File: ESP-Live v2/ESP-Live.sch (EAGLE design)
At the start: 34 parts, among them CN1 USBSMD, IC2 AP2210K-3.3TRG1, IC3 ESP-12F, Y1 RESONATORSMD

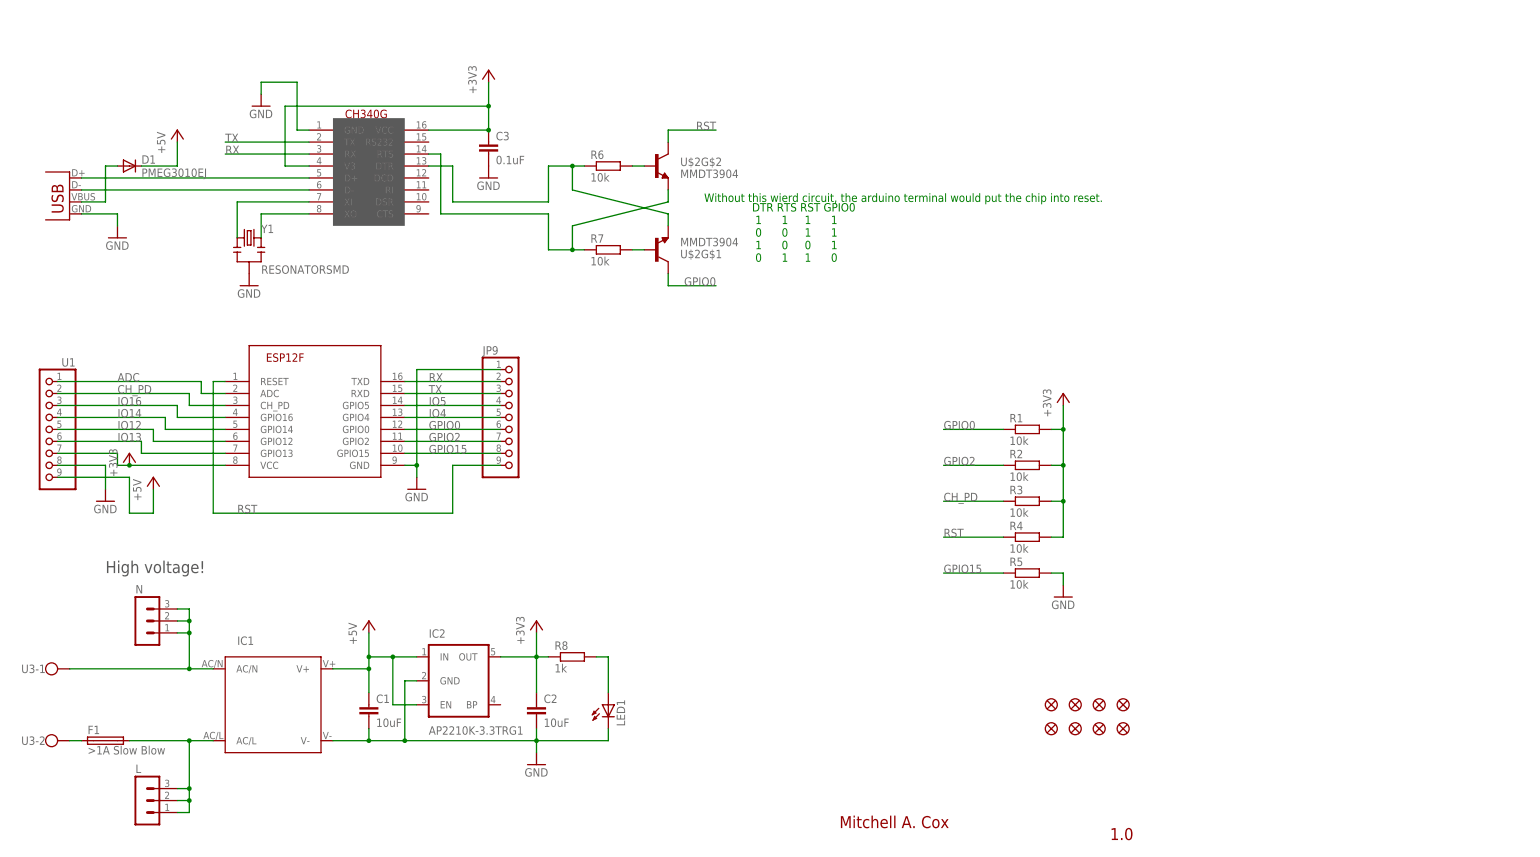
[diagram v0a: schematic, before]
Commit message: with batery charger
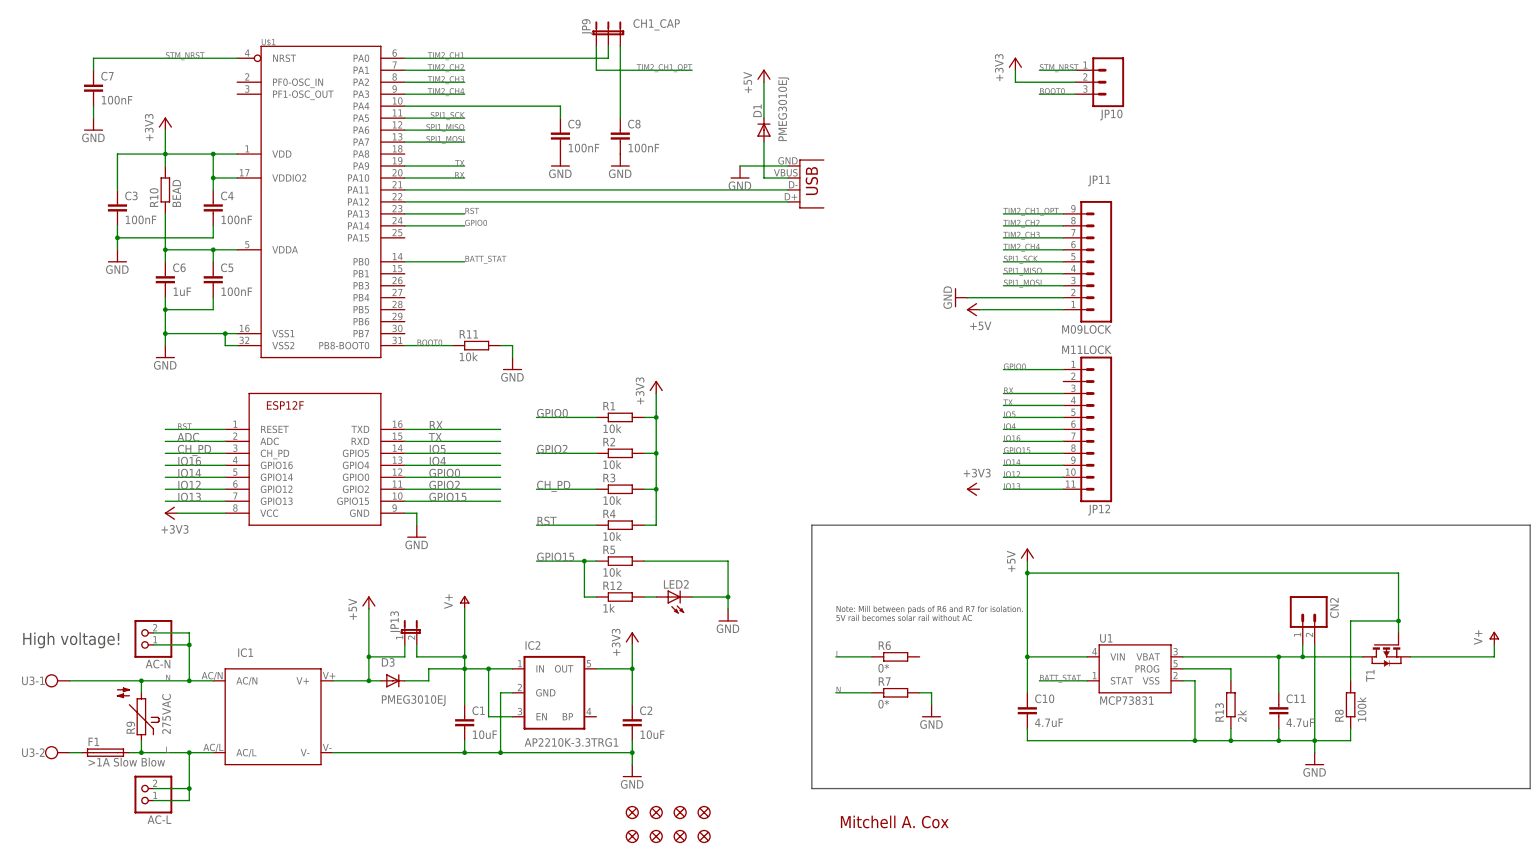
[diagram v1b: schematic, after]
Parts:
- removed L, N: (no value), con-lstb:MA03-1
- removed LED1: (no value), adafruit:LEDCHIPLED_0805
- removed U$2: MMDT3904, SparkFun:MMDT3904
- removed Y1: RESONATORSMD, SparkFun:RESONATORSMD
- added AC-L, AC-N: (no value), pinhead:PINHD-1X2
- added C10, C11: 4.7uF, rcl:C-EUC0805
- added C4, C5, C7, C8, C9: 100nF, rcl:C-EUC0603
- added C6: 1uF, rcl:C-EUC0805
- added CN2: (no value), SparkFun:M02-JST-2-PTH-NO_SILK
- added D3: PMEG3010EJ, SparkFun:DIODESOD
- added JP10: (no value), SparkFun:M03LOCK
- added JP11: M09LOCK, SparkFun:M09LOCK
- added JP12: M11LOCK, SparkFun:M11LOCK
- added JP13: (no value), SparkFun:JUMPER-2SMD-NO
- added LED2: (no value), adafruit:LEDCHIPLED_0805
- added R10: BEAD, rcl:R-EU_R0603
- added R11: 10k, rcl:R-EU_R0603
- added R12: 1k, rcl:R-EU_R0603
- added R13: 2k, rcl:R-EU_R0603
- added R9: 275VAC, varistor:P593
- added T1: (no value), zetex:PMOSSOT23
- C3: value 0.1uF -> 100nF; device rcl:C-EUC0805 -> rcl:C-EUC0603
- JP9: value (none) -> CH1_CAP; device adafruit:PINHD-1X9 -> SparkFun:JUMPER-31-2
- R1, R2, R3, R4, R5: device rcl:R-EU_M0805 -> rcl:R-EU_R0603
- R6, R7: value 10k -> 0*; device rcl:R-EU_M0805 -> rcl:R-EU_R2512
- R8: value 1k -> 100k; device rcl:R-EU_M0805 -> rcl:R-EU_R0603
- U$1: value CH340G -> STM32F042K; device usb-serial:CH340G -> stm32:STM32F042K
- U1: value (none) -> MCP73831; device adafruit:PINHD-1X9 -> SparkFun:MCP73831
- U3: device con-wago-500:W237-113 -> con-wago-500:W237-102
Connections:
- removed net N$15: R7.1, U$1.RTS, U$2G$2.E
- removed net N$16: CN1.D-, U$1.D-
- removed net N$21: U$1.XI, Y1.1
- removed net N$22: U$1.XO, Y1.3
- removed net N$4: LED1.A, R8.2
- removed net N$8: R7.2, U$2G$1.B
- new net BATT_STAT: U$1.PB0, U1.STAT
- new net BOOT0: JP10.3, R11.1, U$1.PB8-BOOT0
- new net L: AC-L.1, AC-L.2, F1.2, IC1.AC/L, R6.1, R9.1
- new net N: AC-N.1, AC-N.2, IC1.AC/N, R7.1, R9.2, U3-1.KL
- new net N$13: C11.1, CN2.1, T1.D, U1.VBAT
- new net N$6: CN1.D-, U$1.PA11
- new net N$7: CN1.D+, U$1.PA12
- new net SPI1_MISO: JP11.4, U$1.PA6
- new net SPI1_MOSI: JP11.3, U$1.PA7
- new net SPI1_SCK: JP11.5, U$1.PA5
- new net STM_NRST: C7.1, JP10.1, U$1.NRST
- new net TIM2_CH1: JP9.2, U$1.PA0
- new net TIM2_CH1_OPT: JP11.9, JP9.1
- new net TIM2_CH2: JP11.8, U$1.PA1
- new net TIM2_CH3: JP11.7, U$1.PA2
- new net TIM2_CH4: JP11.6, U$1.PA3
- new net V+: C1.1, D3.C, IC2.EN, IC2.IN, JP13.2, T1.S
- net +3V3: now also C4.1, JP10.2, R10.2, U$1.VDD, U$1.VDDIO2; no longer R8.1, U$1.V3, U$1.VCC, U1.7
- net +5V: now also C10.1, D3.A, JP11.1, JP13.1, R8.2, T1.G, U1.VIN; no longer C1.1, IC2.EN, IC2.IN, U1.9
- net ADC: no longer U1.1
- net CH_PD: no longer U1.2
- net GND: now also C10.2, C11.2, C4.2, C5.2, C6.2, C7.2, C8.2, C9.2, CN2.2, JP11.2, LED2.C, R11.2, R13.1, R7.2, R8.1, U$1.VSS1, U$1.VSS2, U1.VSS; no longer JP9.1, LED1.C, U$1.GND, U1.8, Y1.2
- net GPIO0: now also JP12.1, U$1.PA14; no longer JP9.6, U$2G$1.C
- net GPIO15: now also JP12.8, R12.1; no longer JP9.8
- net GPIO2: no longer JP9.7
- net IO12: now also JP12.10; no longer U1.5
- net IO13: now also JP12.11; no longer U1.6
- net IO14: now also JP12.9; no longer U1.4
- net IO16: now also JP12.7; no longer U1.3
- net IO4: now also JP12.6; no longer JP9.5
- net IO5: now also JP12.5; no longer JP9.4
- net N$10: now also LED2.A, R12.2; no longer R6.2, U$2G$2.B
- net N$11: now also C9.1, U$1.PA4; no longer R6.1, U$1.DTR, U$2G$1.E
- net N$12: now also C8.1, JP9.3; no longer CN1.D+, U$1.D+
- net N$2: now also C5.1, C6.1, R10.1, U$1.VDDA; no longer IC1.AC/N, N.1, N.2, N.3, U3-1.KL
- net N$3: now also R13.2, U1.PROG; no longer F1.2, IC1.AC/L, L.1, L.2, L.3
- net RST: now also U$1.PA13; no longer JP9.9, U$2G$2.C
- net RX: now also JP12.3, U$1.PA10; no longer JP9.2, U$1.RX
- net TX: now also JP12.4, U$1.PA9; no longer JP9.3, U$1.TX
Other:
- note added: "1A, 5.5V MAX"
- note added: "Note: Mill between pads of R6 and R7 for isolation. 5V rail becomes solar rail without AC"
- note removed: "1.0"
- note removed: "DTR RTS RST GPIO0 1 1 1 1 0 0 1 1 1 0 0 1 0 1 1 0"
- note removed: "Without this wierd circuit, the arduino terminal would put the chip into reset."
- moved on the sheet: C1, C2, C3, D1, F1, IC1, IC2, R1, R2, R3, R4, R5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
